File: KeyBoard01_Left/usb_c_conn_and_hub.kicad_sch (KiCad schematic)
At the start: 27 parts, among them J1 USB_C_Receptacle_USB2.0, J2 USB_C_Receptacle_USB2.0, U2 TUSB2036, Y1 6MHz

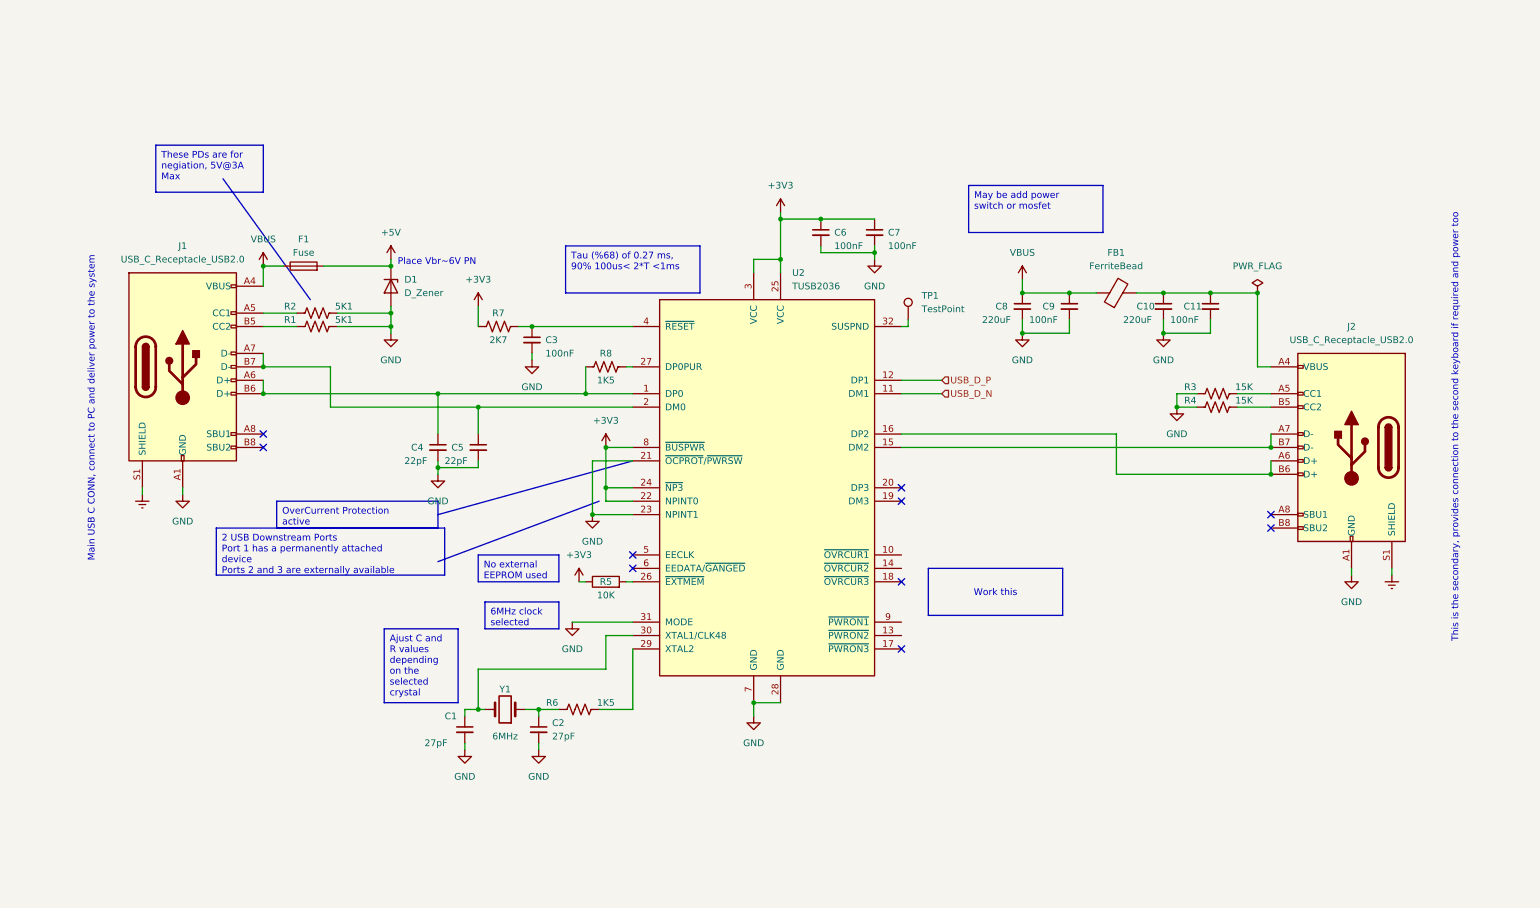
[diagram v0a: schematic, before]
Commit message: USB C CONN: Add 3v3 LDO and USB power en chip
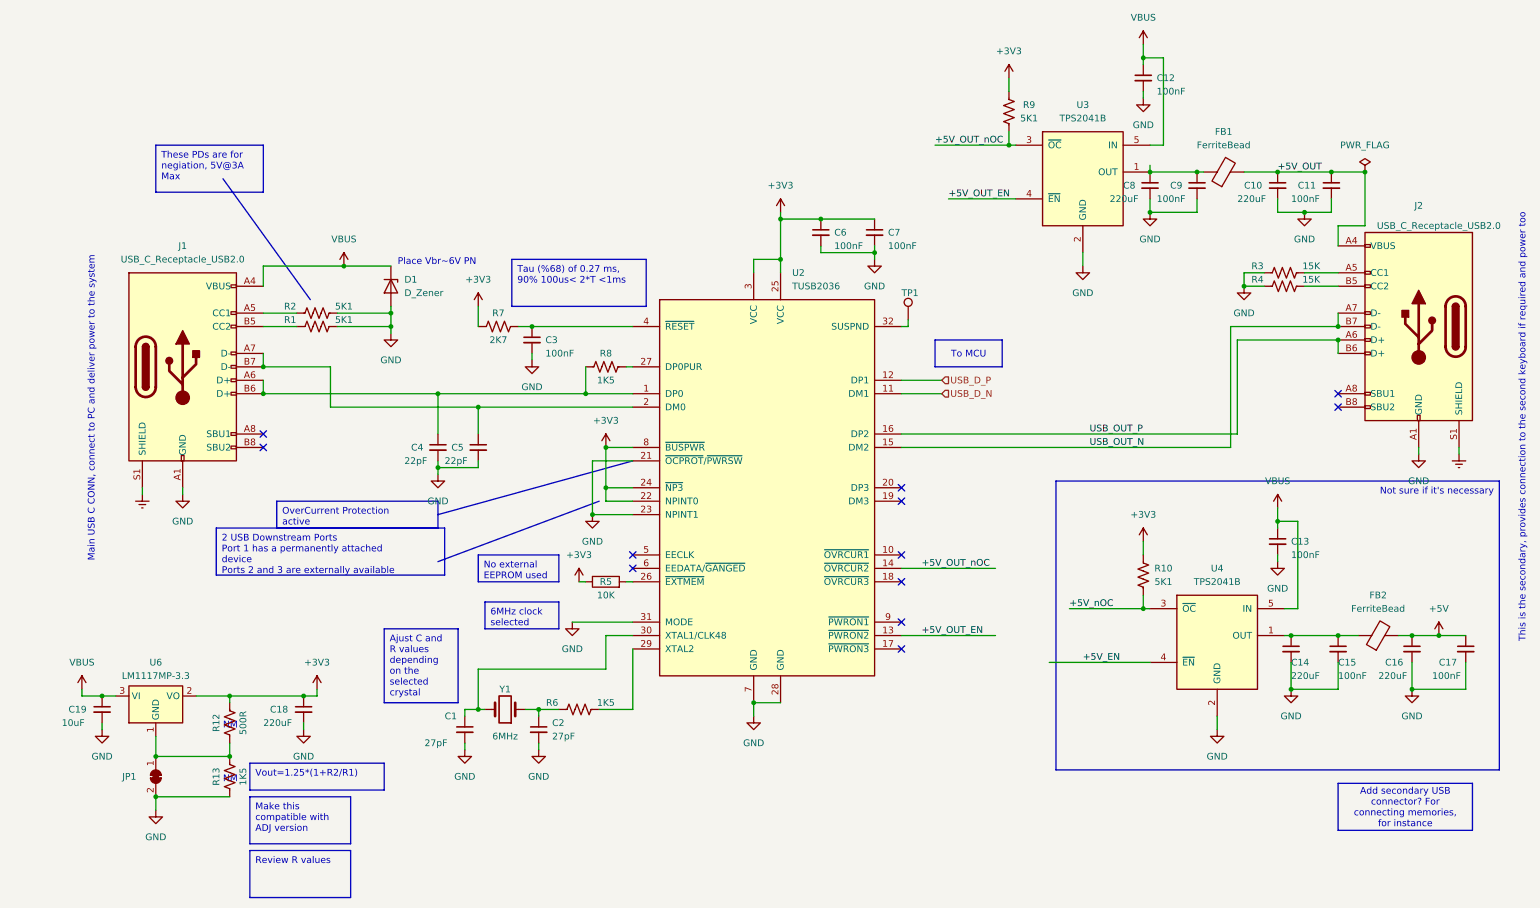
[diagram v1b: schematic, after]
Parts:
- removed F1: Fuse, symbol Device:Fuse
- added C12, C13, C15, C17: 100nF, Capacitor_SMD:C_0402_1005Metric, symbol Device:C_Small
- added C14, C16, C18: 220uF, Capacitor_SMD:C_1206_3216Metric, symbol Device:C_Small
- added C19: 10uF, Capacitor_SMD:C_1206_3216Metric, symbol Device:C_Small
- added FB2: FerriteBead, symbol Device:FerriteBead
- added JP1: SolderJumper_2_Bridged, Jumper:SolderJumper-2_P1.3mm_Bridged2Bar_Pad1.0x1.5mm, symbol Jumper:SolderJumper_2_Bridged
- added R10, R9: 5K1, Resistor_SMD:R_0402_1005Metric, symbol Device:R_US
- added R12: 500R, Resistor_SMD:R_0402_1005Metric, symbol Device:R_US
- added R13: 1K5, Resistor_SMD:R_0402_1005Metric, symbol Device:R_US
- added U3, U4: TPS2041B, Package_TO_SOT_SMD:SOT-23-5, symbol Power_Management:TPS2041B
- added U6: LM1117MP-3.3, Package_TO_SOT_SMD:SOT-223-3_TabPin2, symbol Regulator_Linear:LM1117MP-3.3
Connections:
- net +3V3: now also C18.1, R10.2, R12.1, R9.2, U6.2 (VO)
- net +5V: now also C16.1, C17.1, FB2.2; no longer D1.1 (K)
- net GND: now also C12.2, C13.2, C14.2, C15.2, C16.2, C17.2, C18.2, C19.2, JP1.2 (B), R13.2, U3.2 (GND), U4.2 (GND)
- net VBUS: now also D1.1 (K), C12.1, C13.1, C19.1, U3.5 (IN), U4.5 (IN), U6.3 (VI); no longer C8.1, C9.1, FB1.1
- net +5V_OUT: now reaches C10.1, C11.1, FB1.2, J2.A4 (VBUS), J2.A9 (VBUS), J2.B4 (VBUS), J2.B9 (VBUS)
- net USB_OUT_P: now reaches J2.A6 (D+), J2.B6 (D+), U2.16 (DP2)
- net USB_OUT_N: now reaches J2.A7 (D-), J2.B7 (D-), U2.15 (DM2)
- net +5V_OUT_EN: now reaches U2.13 (~{PWRON2})
- net +5V_OUT_EN: now also U3.4 (~{EN})
- net +5V_OUT_nOC: now reaches U2.14 (~{OVRCUR2})
- net +5V_OUT_nOC: now also R9.1, U3.3 (~{OC})
- new net: C8.1, C9.1, FB1.1, U3.1 (OUT)
- new net: C14.1, C15.1, FB2.1, U4.1 (OUT)
- new net: JP1.1 (A), R12.2, R13.1, U6.1 (GND)
- new net +5V_EN: U4.4 (~{EN})
- new net +5V_nOC: R10.1, U4.3 (~{OC})
- no-connect marks 10 -> 12
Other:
- note added: "NM"
- moved on the sheet: C10, C11, C8, C9, FB1, J2, R3, R4

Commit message: SCH: USB HUB add protection TVSs
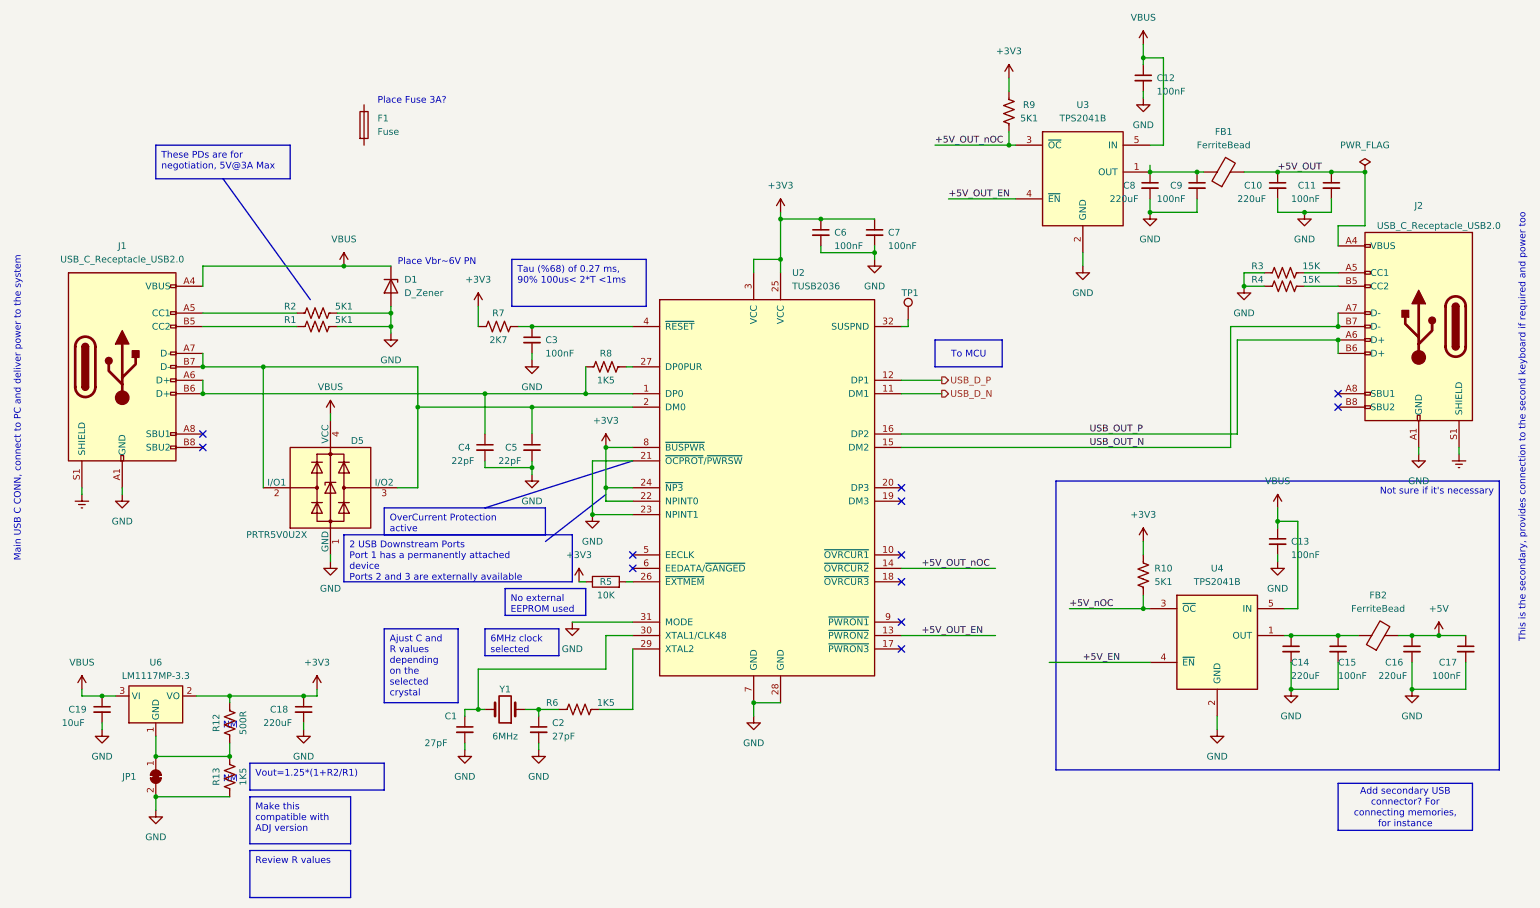
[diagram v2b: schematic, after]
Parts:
- added D5: PRTR5V0U2X, Package_TO_SOT_SMD:SOT-143, symbol Power_Protection:PRTR5V0U2X
- added F1: Fuse, symbol Device:Fuse
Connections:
- net GND: now also D5.1 (GND)
- net VBUS: now also D5.4 (VCC)
- net at C5.1, J1.A7 (D-), J1.B7 (D-)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: now also D5.2 (I/O1), D5.3 (I/O2)
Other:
- note added: "Place Fuse 3A?"
- moved on the sheet: C4, C5, J1

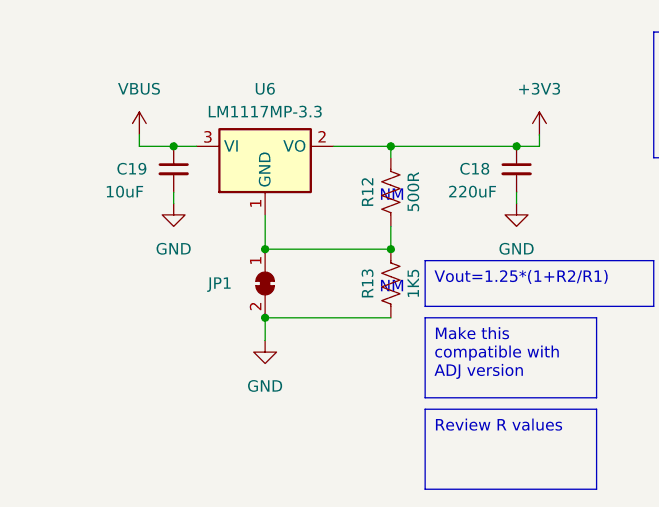
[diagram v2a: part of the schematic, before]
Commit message: USB CONN HUB: Replace jumper for 0R
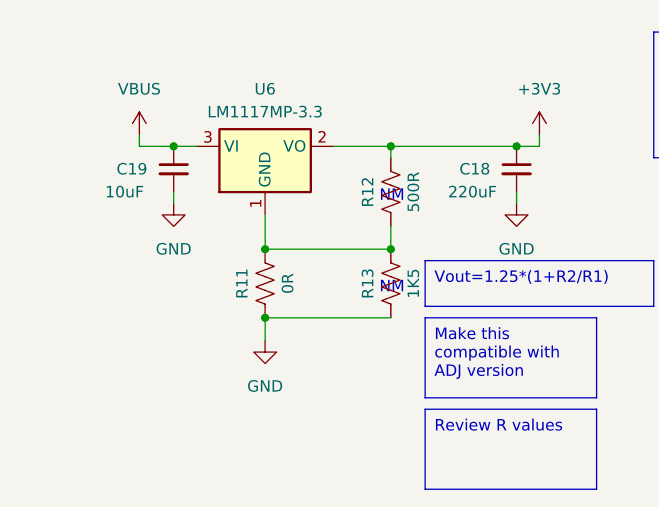
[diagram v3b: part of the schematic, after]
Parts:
- removed JP1: SolderJumper_2_Bridged, Jumper:SolderJumper-2_P1.3mm_Bridged2Bar_Pad1.0x1.5mm, symbol Jumper:SolderJumper_2_Bridged
- added R11: 0R, Resistor_SMD:R_0402_1005Metric, symbol Device:R_US
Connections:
- net GND: now also R11.2
- net at R12.2, R13.1, U6.1 (GND): now also R11.1
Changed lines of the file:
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@@
   (junction (at 104.14 86.36) (diameter 0) (color 0 0 0 0)
   )
+  (junction (at 33.02 152.4) (diameter 0) (color 0 0 0 0)
+  )
   (junction (at 229.87 41.91) (diameter 0) (color 0 0 0 0)
   )
@@
   (junction (at 261.62 41.91) (diameter 0) (color 0 0 0 0)
   )
-  (junction (at 33.02 152.4) (diameter 0) (color 0 0 0 0)
-  )
   (junction (at 41.91 83.82) (diameter 0) (color 0 0 0 0)
   )
+  (junction (at 219.71 20.32) (diameter 0) (color 0 0 0 0)
+  )
+  (junction (at 220.98 41.91) (diameter 0) (color 0 0 0 0)
+  )
+  (junction (at 118.11 101.6) (diameter 0) (color 0 0 0 0)
+  )
+  (junction (at 194.31 36.83) (diameter 0) (color 0 0 0 0)
+  )
+  (junction (at 247.65 129.54) (diameter 0) (color 0 0 0 0)
+  )
+  (junction (at 68.58 59.69) (diameter 0) (color 0 0 0 0)
+  )
+  (junction (at 275.59 129.54) (diameter 0) (color 0 0 0 0)
+  )
   (junction (at 33.02 160.02) (diameter 0) (color 0 0 0 0)
-  )
-  (junction (at 219.71 20.32) (diameter 0) (color 0 0 0 0)
-  )
-  (junction (at 220.98 41.91) (diameter 0) (color 0 0 0 0)
-  )
-  (junction (at 118.11 101.6) (diameter 0) (color 0 0 0 0)
-  )
-  (junction (at 194.31 36.83) (diameter 0) (color 0 0 0 0)
-  )
-  (junction (at 247.65 129.54) (diameter 0) (color 0 0 0 0)
-  )
-  (junction (at 68.58 59.69) (diameter 0) (color 0 0 0 0)
-  )
-  (junction (at 275.59 129.54) (diameter 0) (color 0 0 0 0)
   )
   (junction (at 256.54 129.54) (diameter 0) (color 0 0 0 0)
@@
     )
   )
-  (symbol (lib_id "Jumper:SolderJumper_2_Bridged") (at 33.02 156.21 270) (unit 1)
-    (in_bom yes) (on_board yes) (dnp no)
-    (property "Reference" "JP1" (at 26.67 156.21 90)
-      (effects (font (size 1.27 1.27)) (justify left))
-    )
-    (property "Value" "SolderJumper_2_Bridged" (at 19.05 161.29 90)
-      (effects (font (size 1.27 1.27)) (justify left) hide)
-    )
-    (property "Footprint" "Jumper:SolderJumper-2_P1.3mm_Bridged2Bar_Pad1.0x1.5mm" (at 33.02 156.21 0)
-      (effects (font (size 1.27 1.27)) hide)
-    )
-    (property "Datasheet" "~" (at 33.02 156.21 0)
-      (effects (font (size 1.27 1.27)) hide)
-    )
-    (pin "2")
-    (pin "1")
-    (instances
-      (project "KeyBoard01_Left"
-        (path "/30001e54-b931-4c99-a85a-cc67ed27d667/9cc5f9c6-3c68-4ae5-a9ab-38645611b9ab"
-          (reference "JP1") (unit 1)
-        )
-      )
-    )
-  )
   (symbol (lib_id "Device:Crystal") (at 99.06 143.51 180) (unit 1)
     (in_bom yes) (on_board yes) (dnp no)
@@
         )
       )
+    )
+  )
+  (symbol (lib_id "Device:R_US") (at 33.02 156.21 0) (unit 1)
+    (in_bom yes) (on_board yes) (dnp no)
+    (property "Reference" "R11" (at 30.48 156.21 90)
+      (effects (font (size 1.27 1.27)))
+    )
+    (property "Value" "0R" (at 35.56 156.21 90)
+      (effects (font (size 1.27 1.27)))
+    )
+    (property "Footprint" "Resistor_SMD:R_0402_1005Metric" (at 34.036 156.464 90)
+      (effects (font (size 1.27 1.27)) hide)
+    )
+    (property "Datasheet" "~" (at 33.02 156.21 0)
+      (effects (font (size 1.27 1.27)) hide)
+    )
+    (pin "1")
+    (pin "2")
+    (instances
+      (project "KeyBoard01_Left"
+        (path "/30001e54-b931-4c99-a85a-cc67ed27d667/9cc5f9c6-3c68-4ae5-a9ab-38645611b9ab"
+          (reference "R11") (unit 1)
+        )
+      )
